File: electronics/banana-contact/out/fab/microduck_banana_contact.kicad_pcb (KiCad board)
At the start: 2 copper layers, 45.8 x 5.1 mm, 2 parts, among them P1 NP-F pack contacts, P2 3-wire tail to the HAT

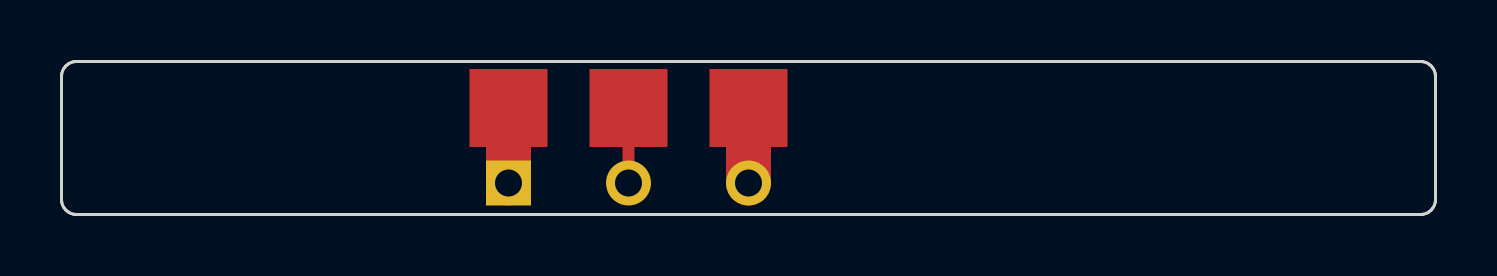
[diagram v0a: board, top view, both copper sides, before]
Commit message: lane D: the banana board's pocket was measured with the wrong ceiling
Ray-cast the power_support solid on a 2 mm grid at y = 31.000, mid-gap, instead
of reading section outlines. The map is unambiguous: above z = 51.000 the only
material is the two screw posts at x = +/-25, so the pocket is OPEN UPWARD and
the head plate is BEHIND the board, not above it. The plate's top edge is also
curved - 56.944 mm at x ~ +4, 55.51 at x +/-24 - so no single number off one
section was ever the ceiling, and the 56.080 read at x = 20 was an artefact of
where the section was taken.

The real ceiling is the locker bar's own silhouette, z 48.974..55.626: a board
taller than its retainer is a board the retainer does not cover. The pocket is
46.292 x 4.696 (x bounded by the posts' inner faces at +/-23.146), so the board
is now 45.800 x 4.600 and enters with 0.246 mm per side in x and 0.048 in z.
The 5.100 mm board would have stood 0.404 mm proud of its own retainer.
Contacts 2.400 mm square, tail holes 0.800 mm dia with a 0.300 mm ring.
DRC CANNOT DETERMINE - 12 pass, 0 fail, 3 undetermined - all three named.
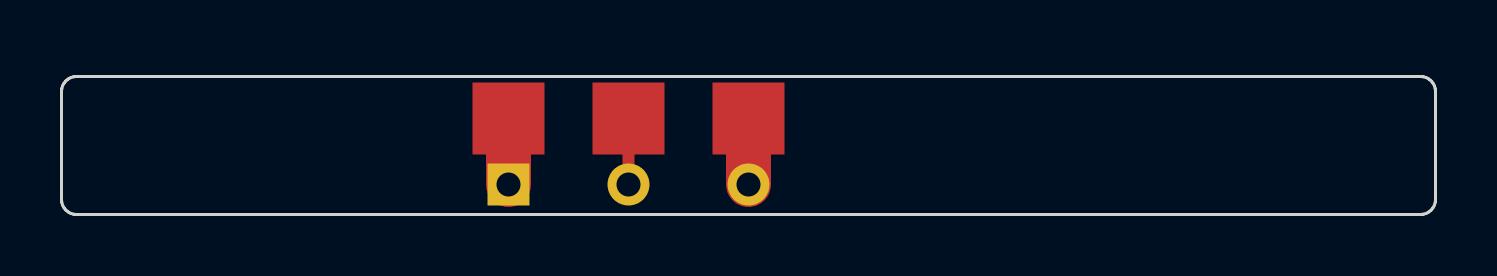
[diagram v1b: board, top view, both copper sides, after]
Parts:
- moved P1 0.35 mm to (18.9, -3.20)
- moved P2 0.05 mm to (18.9, -1.00)
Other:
- board size 45.8 x 5.1 mm -> 45.8 x 4.6 mm
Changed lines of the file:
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@@
   (net 3 "VBAT")
   (footprint "npf-contact-3" (layer "F.Cu")
-    (at 18.9000 -3.5500 0.00)
+    (at 18.9000 -3.2000 0.00)
     (fp_text reference "P1" (at 0 -1) (layer "F.Silk"))
     (fp_text value "NP-F pack contacts" (at 0 1) (layer "F.Silk") hide)
-    (pad "BAT+" smd rect (at -4.0000 -0.0000 0.00) (size 2.6000 2.6000) (layers "F.Cu" "F.Mask" "F.Paste") (net 3 "VBAT"))
-    (pad "T" smd rect (at 0.0000 -0.0000 0.00) (size 2.6000 2.6000) (layers "F.Cu" "F.Mask" "F.Paste") (net 1 "BAT_T"))
-    (pad "BAT-" smd rect (at 4.0000 -0.0000 0.00) (size 2.6000 2.6000) (layers "F.Cu" "F.Mask" "F.Paste") (net 2 "GND"))
+    (pad "BAT+" smd rect (at -4.0000 -0.0000 0.00) (size 2.4000 2.4000) (layers "F.Cu" "F.Mask" "F.Paste") (net 3 "VBAT"))
+    (pad "T" smd rect (at 0.0000 -0.0000 0.00) (size 2.4000 2.4000) (layers "F.Cu" "F.Mask" "F.Paste") (net 1 "BAT_T"))
+    (pad "BAT-" smd rect (at 4.0000 -0.0000 0.00) (size 2.4000 2.4000) (layers "F.Cu" "F.Mask" "F.Paste") (net 2 "GND"))
   )
   (footprint "wire-tail-3" (layer "F.Cu")
-    (at 18.9000 -1.0500 0.00)
+    (at 18.9000 -1.0000 0.00)
     (fp_text reference "P2" (at 0 -1) (layer "F.Silk"))
     (fp_text value "3-wire tail to the HAT" (at 0 1) (layer "F.Silk") hide)
-    (pad "BAT+" thru_hole rect (at -4.0000 -0.0000 0.00) (size 1.5000 1.5000) (drill 0.9) (layers "*.Cu" "*.Mask") (net 3 "VBAT"))
-    (pad "T" thru_hole circle (at 0.0000 -0.0000 0.00) (size 1.5000 1.5000) (drill 0.9) (layers "*.Cu" "*.Mask") (net 1 "BAT_T"))
-    (pad "BAT-" thru_hole circle (at 4.0000 -0.0000 0.00) (size 1.5000 1.5000) (drill 0.9) (layers "*.Cu" "*.Mask") (net 2 "GND"))
+    (pad "BAT+" thru_hole rect (at -4.0000 -0.0000 0.00) (size 1.4000 1.4000) (drill 0.8) (layers "*.Cu" "*.Mask") (net 3 "VBAT"))
+    (pad "T" thru_hole circle (at 0.0000 -0.0000 0.00) (size 1.4000 1.4000) (drill 0.8) (layers "*.Cu" "*.Mask") (net 1 "BAT_T"))
+    (pad "BAT-" thru_hole circle (at 4.0000 -0.0000 0.00) (size 1.4000 1.4000) (drill 0.8) (layers "*.Cu" "*.Mask") (net 2 "GND"))
   )
   (gr_line (start 45.3000 -0.0000) (end 45.3975 -0.0096) (stroke (width 0.1) (type solid)) (layer "Edge.Cuts"))
@@
   (gr_line (start 45.7619 -0.3087) (end 45.7904 -0.4025) (stroke (width 0.1) (type solid)) (layer "Edge.Cuts"))
   (gr_line (start 45.7904 -0.4025) (end 45.8000 -0.5000) (stroke (width 0.1) (type solid)) (layer "Edge.Cuts"))
-  (gr_line (start 45.8000 -0.5000) (end 45.8000 -4.6000) (stroke (width 0.1) (type solid)) (layer "Edge.Cuts"))
-  (gr_line (start 45.8000 -4.6000) (end 45.7904 -4.6975) (stroke (width 0.1) (type solid)) (layer "Edge.Cuts"))
-  (gr_line (start 45.7904 -4.6975) (end 45.7619 -4.7913) (stroke (width 0.1) (type solid)) (layer "Edge.Cuts"))
-  (gr_line (start 45.7619 -4.7913) (end 45.7157 -4.8778) (stroke (width 0.1) (type solid)) (layer "Edge.Cuts"))
-  (gr_line (start 45.7157 -4.8778) (end 45.6536 -4.9536) (stroke (width 0.1) (type solid)) (layer "Edge.Cuts"))
-  (gr_line (start 45.6536 -4.9536) (end 45.5778 -5.0157) (stroke (width 0.1) (type solid)) (layer "Edge.Cuts"))
-  (gr_line (start 45.5778 -5.0157) (end 45.4913 -5.0619) (stroke (width 0.1) (type solid)) (layer "Edge.Cuts"))
-  (gr_line (start 45.4913 -5.0619) (end 45.3975 -5.0904) (stroke (width 0.1) (type solid)) (layer "Edge.Cuts"))
-  (gr_line (start 45.3975 -5.0904) (end 45.3000 -5.1000) (stroke (width 0.1) (type solid)) (layer "Edge.Cuts"))
-  (gr_line (start 45.3000 -5.1000) (end 0.5000 -5.1000) (stroke (width 0.1) (type solid)) (layer "Edge.Cuts"))
-  (gr_line (start 0.5000 -5.1000) (end 0.4025 -5.0904) (stroke (width 0.1) (type solid)) (layer "Edge.Cuts"))
-  (gr_line (start 0.4025 -5.0904) (end 0.3087 -5.0619) (stroke (width 0.1) (type solid)) (layer "Edge.Cuts"))
-  (gr_line (start 0.3087 -5.0619) (end 0.2222 -5.0157) (stroke (width 0.1) (type solid)) (layer "Edge.Cuts"))
-  (gr_line (start 0.2222 -5.0157) (end 0.1464 -4.9536) (stroke (width 0.1) (type solid)) (layer "Edge.Cuts"))
-  (gr_line (start 0.1464 -4.9536) (end 0.0843 -4.8778) (stroke (width 0.1) (type solid)) (layer "Edge.Cuts"))
-  (gr_line (start 0.0843 -4.8778) (end 0.0381 -4.7913) (stroke (width 0.1) (type solid)) (layer "Edge.Cuts"))
-  (gr_line (start 0.0381 -4.7913) (end 0.0096 -4.6975) (stroke (width 0.1) (type solid)) (layer "Edge.Cuts"))
-  (gr_line (start 0.0096 -4.6975) (end 0.0000 -4.6000) (stroke (width 0.1) (type solid)) (layer "Edge.Cuts"))
-  (gr_line (start 0.0000 -4.6000) (end 0.0000 -0.5000) (stroke (width 0.1) (type solid)) (layer "Edge.Cuts"))
+  (gr_line (start 45.8000 -0.5000) (end 45.8000 -4.1000) (stroke (width 0.1) (type solid)) (layer "Edge.Cuts"))
+  (gr_line (start 45.8000 -4.1000) (end 45.7904 -4.1975) (stroke (width 0.1) (type solid)) (layer "Edge.Cuts"))
+  (gr_line (start 45.7904 -4.1975) (end 45.7619 -4.2913) (stroke (width 0.1) (type solid)) (layer "Edge.Cuts"))
+  (gr_line (start 45.7619 -4.2913) (end 45.7157 -4.3778) (stroke (width 0.1) (type solid)) (layer "Edge.Cuts"))
+  (gr_line (start 45.7157 -4.3778) (end 45.6536 -4.4536) (stroke (width 0.1) (type solid)) (layer "Edge.Cuts"))
+  (gr_line (start 45.6536 -4.4536) (end 45.5778 -4.5157) (stroke (width 0.1) (type solid)) (layer "Edge.Cuts"))
+  (gr_line (start 45.5778 -4.5157) (end 45.4913 -4.5619) (stroke (width 0.1) (type solid)) (layer "Edge.Cuts"))
+  (gr_line (start 45.4913 -4.5619) (end 45.3975 -4.5904) (stroke (width 0.1) (type solid)) (layer "Edge.Cuts"))
+  (gr_line (start 45.3975 -4.5904) (end 45.3000 -4.6000) (stroke (width 0.1) (type solid)) (layer "Edge.Cuts"))
+  (gr_line (start 45.3000 -4.6000) (end 0.5000 -4.6000) (stroke (width 0.1) (type solid)) (layer "Edge.Cuts"))
+  (gr_line (start 0.5000 -4.6000) (end 0.4025 -4.5904) (stroke (width 0.1) (type solid)) (layer "Edge.Cuts"))
+  (gr_line (start 0.4025 -4.5904) (end 0.3087 -4.5619) (stroke (width 0.1) (type solid)) (layer "Edge.Cuts"))
+  (gr_line (start 0.3087 -4.5619) (end 0.2222 -4.5157) (stroke (width 0.1) (type solid)) (layer "Edge.Cuts"))
+  (gr_line (start 0.2222 -4.5157) (end 0.1464 -4.4536) (stroke (width 0.1) (type solid)) (layer "Edge.Cuts"))
+  (gr_line (start 0.1464 -4.4536) (end 0.0843 -4.3778) (stroke (width 0.1) (type solid)) (layer "Edge.Cuts"))
+  (gr_line (start 0.0843 -4.3778) (end 0.0381 -4.2913) (stroke (width 0.1) (type solid)) (layer "Edge.Cuts"))
+  (gr_line (start 0.0381 -4.2913) (end 0.0096 -4.1975) (stroke (width 0.1) (type solid)) (layer "Edge.Cuts"))
+  (gr_line (start 0.0096 -4.1975) (end 0.0000 -4.1000) (stroke (width 0.1) (type solid)) (layer "Edge.Cuts"))
+  (gr_line (start 0.0000 -4.1000) (end 0.0000 -0.5000) (stroke (width 0.1) (type solid)) (layer "Edge.Cuts"))
   (gr_line (start 0.0000 -0.5000) (end 0.0096 -0.4025) (stroke (width 0.1) (type solid)) (layer "Edge.Cuts"))
   (gr_line (start 0.0096 -0.4025) (end 0.0381 -0.3087) (stroke (width 0.1) (type solid)) (layer "Edge.Cuts"))
@@
   (gr_line (start 0.4025 -0.0096) (end 0.5000 -0.0000) (stroke (width 0.1) (type solid)) (layer "Edge.Cuts"))
   (gr_line (start 0.5000 -0.0000) (end 45.3000 -0.0000) (stroke (width 0.1) (type solid)) (layer "Edge.Cuts"))
-  (segment (start 14.9000 -3.5500) (end 14.9000 -1.0500) (width 1.5) (layer "F.Cu") (net 3))
-  (segment (start 22.9000 -3.5500) (end 22.9000 -1.0500) (width 1.5) (layer "F.Cu") (net 2))
-  (segment (start 18.9000 -3.5500) (end 18.9000 -1.0500) (width 0.4) (layer "F.Cu") (net 1))
+  (segment (start 14.9000 -3.2000) (end 14.9000 -1.0000) (width 1.5) (layer "F.Cu") (net 3))
+  (segment (start 22.9000 -3.2000) (end 22.9000 -1.0000) (width 1.5) (layer "F.Cu") (net 2))
+  (segment (start 18.9000 -3.2000) (end 18.9000 -1.0000) (width 0.4) (layer "F.Cu") (net 1))
 )
